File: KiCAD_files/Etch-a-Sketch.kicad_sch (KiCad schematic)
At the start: 45 parts, among them J1 Debug Connector, J2 Display / Mounting Socket, J3 Display Mounting Socket, P1 282837-2, U1 STM32L433CCTx, U2 W25Q64JV, U3 ICM-42688-P, U6 Adafruit 377 Rotary Encoder, U7 Adafruit 377 Rotary Encoder

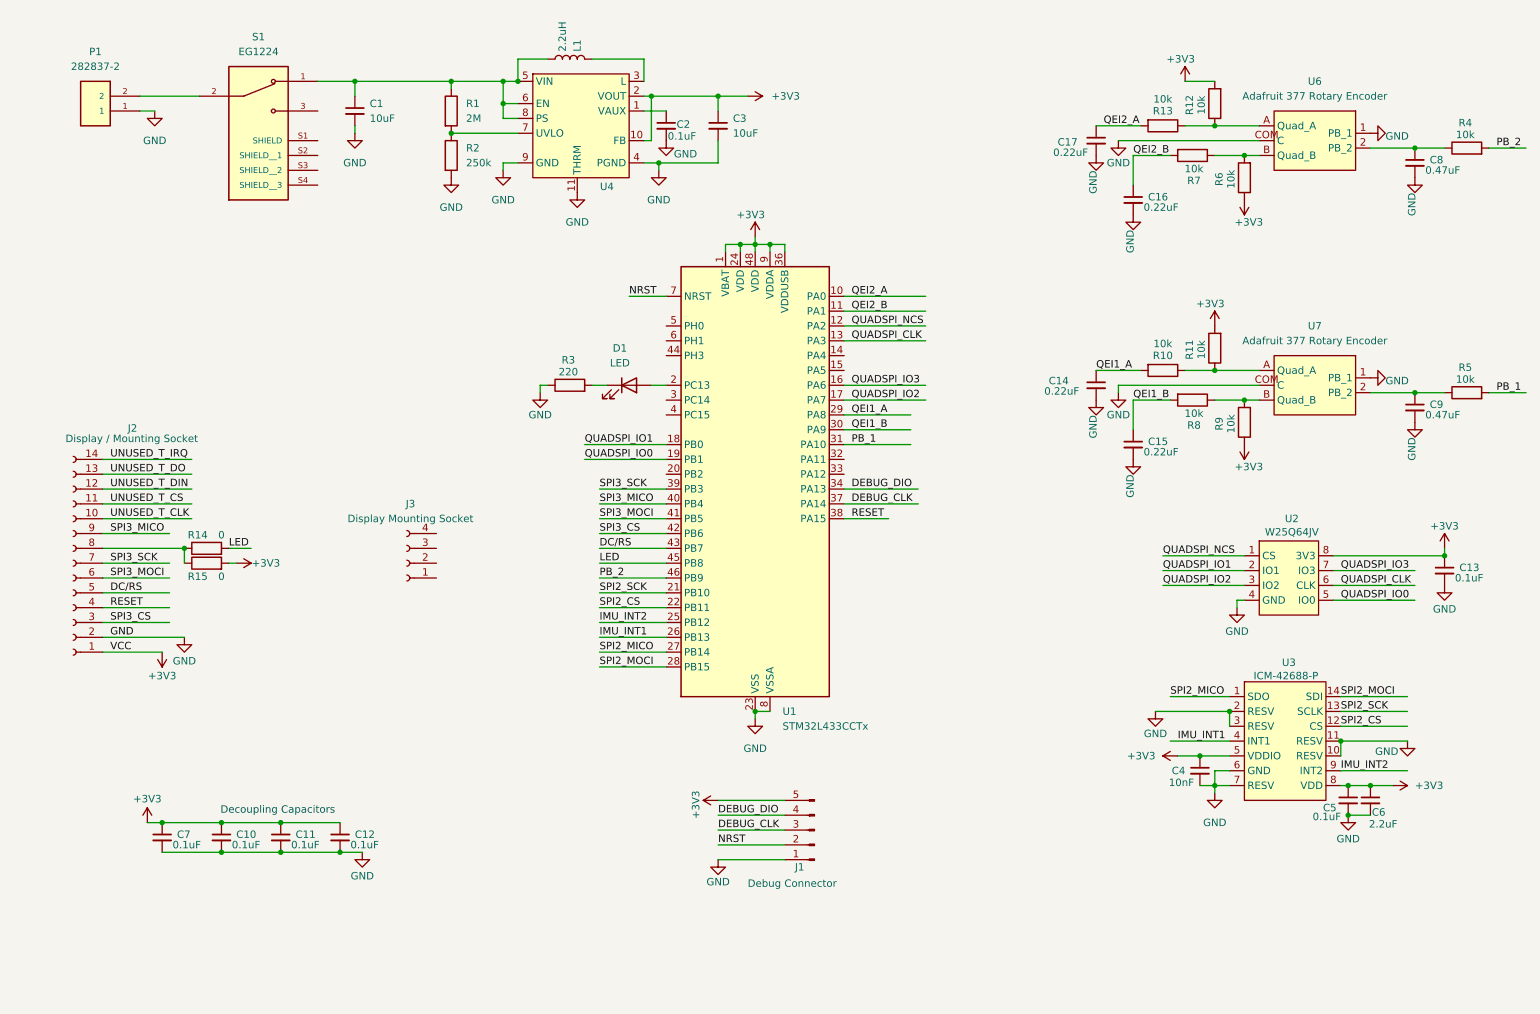
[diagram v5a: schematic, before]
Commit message: Initial Rev1 Changes, including
Mounting holes
Switch to choose backlight reference to replace jumper resistors
Pull ups/downs for NRST and BOOT0
Move the debug connector location
Relabel passive components
Add jumper resistors to remove power from ICs
Add diode to prevent reverse powering
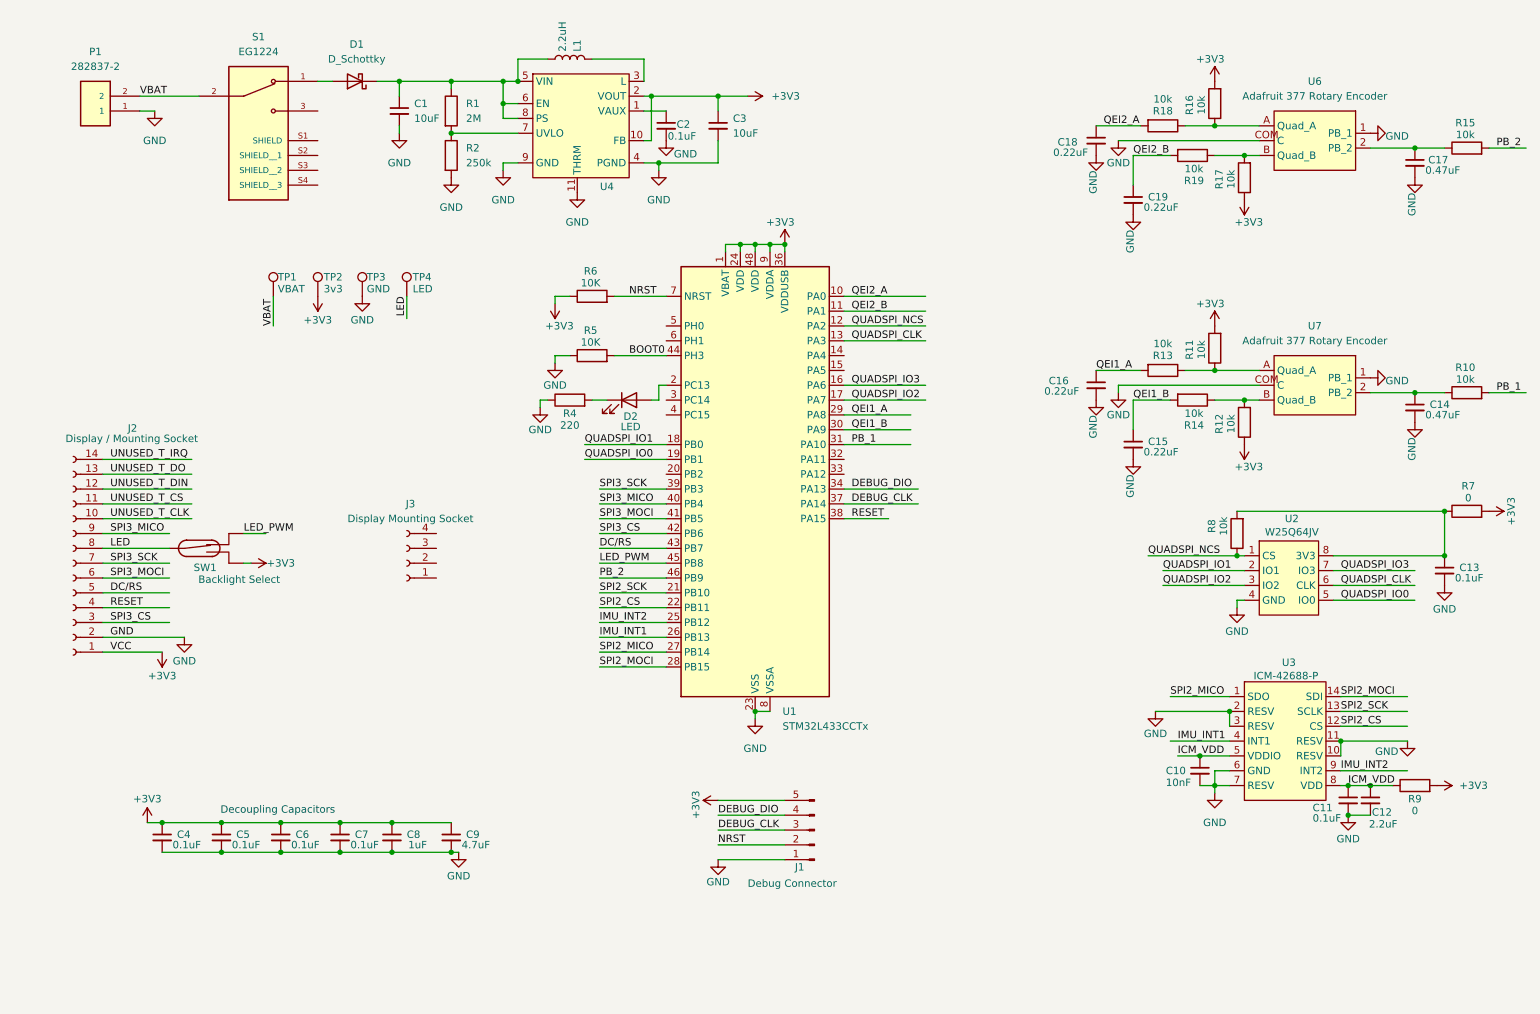
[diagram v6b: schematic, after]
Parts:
- removed R14, R15: 0, Resistor_SMD:R_0603_1608Metric, symbol Device:R
- added C8: 1uF, Capacitor_SMD:C_0603_1608Metric, symbol Device:C_Small
- added C9: 4.7uF, Capacitor_SMD:C_0603_1608Metric, symbol Device:C_Small
- added D1: D_Schottky, Diode_SMD:D_0603_1608Metric, symbol Device:D_Schottky
- added R5, R6: 10K, Resistor_SMD:R_0603_1608Metric, symbol Device:R
- added R7, R9: 0, Resistor_SMD:R_0603_1608Metric, symbol Device:R
- added R8: 10k, Resistor_SMD:R_0603_1608Metric, symbol Device:R
- added SW1: Backlight Select, Switch_footprint:CJS-1200B_NDC, symbol Switch:SW_Reed_SPDT
- added TP1: VBAT, TestPoint:TestPoint_Loop_D1.80mm_Drill1.0mm_Beaded, symbol Connector:TestPoint
- added TP2: 3v3, TestPoint:TestPoint_Loop_D1.80mm_Drill1.0mm_Beaded, symbol Connector:TestPoint
- added TP3: GND, TestPoint:TestPoint_Loop_D1.80mm_Drill1.0mm_Beaded, symbol Connector:TestPoint
- added TP4: LED, TestPoint:TestPoint_Loop_D1.80mm_Drill1.0mm_Beaded, symbol Connector:TestPoint
- D2: renamed from D1; footprint LED_SMD:LED_0201_0603Metric -> LED_SMD:LED_0603_1608Metric
- renumbered C4 to C10, C5 to C11, C6 to C12, C9 to C14, C14 to C16, C8 to C17, C17 to C18, C16 to C19, C7 to C4, C10 to C5, C11 to C6, C12 to C7, R5 to R10, R9 to R12, R10 to R13, R8 to R14, R4 to R15, R12 to R16, R6 to R17, R13 to R18, R7 to R19, R3 to R4
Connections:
- net +3V3: now also C8.1, C9.1, R6.1, R7.2, R9.2, SW1.3, TP2.1; no longer C10.1, C11.1, C12.1, C13.1, U2.8 (3V3), U3.5 (VDDIO), U3.8 (VDD)
- net GND: now also C8.2, C9.2, R5.1, TP3.1
- net LED: now also J2.8 (Pin_8), SW1.2, TP4.1; no longer U1.45 (PB8)
- net NRST: now also R6.2
- net QUADSPI_NCS: now also R8.1
- net at C1.1, L1.2, R1.1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: now also D1.1 (K); no longer S1.1
- net VBAT: now reaches P1.2, S1.2
- net VBAT: now also TP1.1
- net BOOT0: now reaches U1.44 (PH3)
- net BOOT0: now also R5.2
- new net: D1.2 (A), S1.1
- new net: C13.1, R7.1, R8.2, U2.8 (3V3)
- new net ICM_VDD: C10.1, C11.1, C12.1, R9.1, U3.5 (VDDIO), U3.8 (VDD)
- new net LED_PWM: SW1.1, U1.45 (PB8)
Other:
- moved on the sheet: C1, D2, R4

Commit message: Update Schematic to Rev1
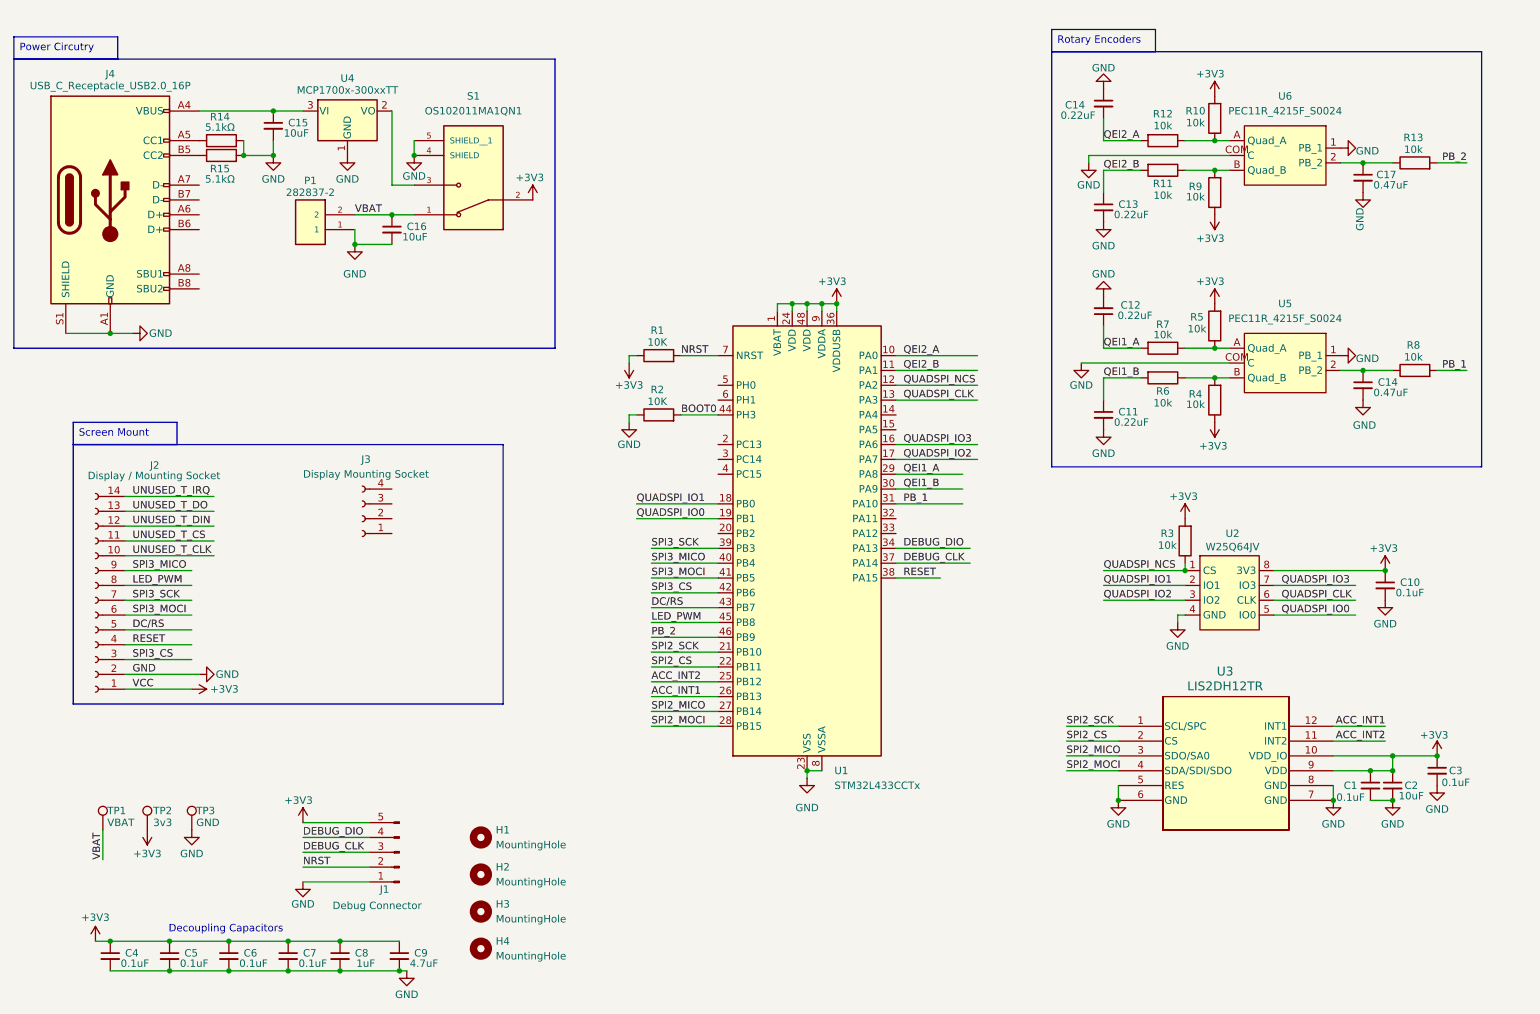
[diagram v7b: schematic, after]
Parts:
- removed C10: 10nF, Capacitor_SMD:C_0603_1608Metric, symbol Device:C_Small
- removed C11: 0.1uF, Capacitor_SMD:C_0603_1608Metric, symbol Device:C_Small
- removed C12: 2.2uF, Capacitor_SMD:C_0603_1608Metric, symbol Device:C_Small
- removed D1: D_Schottky, Diode_SMD:D_0603_1608Metric, symbol Device:D_Schottky
- removed D2: LED, LED_SMD:LED_0603_1608Metric, symbol Device:LED
- removed L1: 2.2uH, LPS3015-222MRC:IND_LPS3015-222MRC, symbol Device:L
- removed R1: 2M, Resistor_SMD:R_0603_1608Metric, symbol Device:R
- removed R2: 250k, Resistor_SMD:R_0603_1608Metric, symbol Device:R
- removed R4: 220, Resistor_SMD:R_0603_1608Metric, symbol Device:R
- removed R7, R9: 0, Resistor_SMD:R_0603_1608Metric, symbol Device:R
- removed SW1: Backlight Select, Switch_footprint:CJS-1200B_NDC, symbol Switch:SW_Reed_SPDT
- removed TP4: LED, TestPoint:TestPoint_Loop_D1.80mm_Drill1.0mm_Beaded, symbol Connector:TestPoint
- removed U3: ICM-42688-P, ICM_42688_P:PQFN50P300X250X97-14N, symbol Etch_a_sketch_components:ICM-42688-P
- removed U4: ~, TPS61201DRCT:VREG_V62_16624-01YE, symbol Etch_a_sketch_components:TPS61201DRC
- added C15, C16: 10uF, Capacitor_SMD:C_0603_1608Metric, symbol Device:C_Small
- added H1, H2, H3, H4: MountingHole, MountingHole:ToolingHole_1.152mm, symbol Mechanical:MountingHole
- added J4: USB_C_Receptacle_USB2.0_16P, symbol Connector:USB_C_Receptacle_USB2.0_16P
- added R14, R15: 5.1kΩ, Resistor_SMD:R_0603_1608Metric, symbol Device:R
- added U3: LIS2DH12TR, LGA-12_STM, symbol LIS2DH12TR:LIS2DH12TR
- added U4: MCP1700x-300xxTT, Package_TO_SOT_SMD:SOT-23, symbol Regulator_Linear:MCP1700x-300xxTT
- C1, C3: value 10uF -> 0.1uF
- C2: value 0.1uF -> 10uF
- S1: value EG1224 -> OS102011MA1QN1
- U5: renamed from U7; value Adafruit 377 Rotary Encoder -> PEC11R_4215F_S0024
- U6: value Adafruit 377 Rotary Encoder -> PEC11R_4215F_S0024
- renumbered C13 to C10, C15 to C11, C16 to C12, C19 to C13, C18 to C14, R6 to R1, R16 to R10, R19 to R11, R18 to R12, R15 to R13, R5 to R2, R8 to R3, R12 to R4, R11 to R5, R14 to R6, R13 to R7, R10 to R8, R17 to R9
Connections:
- net LED is gone; now on net LED_PWM: J2.8 (Pin_8)
- net +3V3: now also C1.1, C10.1, C2.1, R3.2, S1.2, U2.8 (3V3), U3.10 (VDD_IO), U3.9 (VDD)
- net GND: now also C14.1, S1.4 (SHIELD), S1.5 (SHIELD__1), C15.2, C16.2, J4.A1 (GND), J4.A12 (GND), J4.B1 (GND), J4.B12 (GND), J4.S1 (SHIELD), R14.2, R15.2, U3.5 (RES), U3.6 (GND), U3.7 (GND), U3.8 (GND), U4.1 (GND); no longer C14.2
- net QEI2_A: now also C14.2; no longer C14.1
- net SPI2_CS: now also U3.2 (CS)
- net SPI2_MICO: now also U3.3 (SDO/SA0)
- net SPI2_MOCI: now also U3.4 (SDA/SDI/SDO)
- net SPI2_SCK: now also U3.1 (SCL/SPC)
- net VBAT: now also S1.1, C16.1; no longer S1.2
- net at S1.3: now also U4.2 (VO)
- net IMU_INT1 renamed ACC_INT1
- net ACC_INT1: now also U3.12 (INT1)
- net IMU_INT2 renamed ACC_INT2
- net ACC_INT2: now also U3.11 (INT2)
- new net: J4.A5 (CC1), R14.1
- new net: C15.1, J4.A4 (VBUS), J4.A9 (VBUS), J4.B4 (VBUS), J4.B9 (VBUS), U4.3 (VI)
- new net: J4.B5 (CC2), R15.1
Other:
- moved on the sheet: C10, C11, C12, C13, C14, C17, C4, C5, C6, C7, C8, C9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

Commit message: Initial Rev1 PCB Layout
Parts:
- added C18: 1uF, Capacitor_SMD:C_0603_1608Metric, symbol Device:C_Small
- added C20: 0.1uF, Capacitor_SMD:C_0603_1608Metric, symbol Device:C_Small
- C17: renamed from C15; value 10uF -> 1uF
- C7: value 0.1uF -> 10nF
- J1: footprint Connector_PinHeader_2.54mm:PinHeader_1x05_P2.54mm_Horizontal -> Connector_PinHeader_2.54mm:PinHeader_1x05_P2.54mm_Vertical
- J4: value USB_C_Receptacle_USB2.0_16P -> Molex 2171790001; footprint (none) -> Molex2171790001:2171790001_MOL
- S1: footprint EG1224:SW_EG1224 -> OS102011MA1QN1:OS102011MA1QN1_CNK
- renumbered C14 to C13, C13 to C15, C17 to C16, C16 to C19
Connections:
- net +3V3: now also C20.1
- net GND: now also J4.A1/B12 (GND), J4.B1/A12 (GND), U5.S1, U5.S2, U6.S1, U6.S2, C18.2, C20.2; no longer J4.A1 (GND), J4.A12 (GND), J4.B1 (GND), J4.B12 (GND)
- net at S1.3, U4.2 (VO): now also C18.1
- new net: C17.1, J4.A4/B9 (VBUS), J4.B4/A9 (VBUS), U4.3 (VI)
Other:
- moved on the sheet: C13, C16, C17, C19, J2, J3, J4, P1, R13, R14, R15, R8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
